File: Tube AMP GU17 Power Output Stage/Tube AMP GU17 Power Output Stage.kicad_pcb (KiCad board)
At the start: 2 copper layers, 100 x 50 mm, 37 parts, among them J1 AIN+, J10 BRN, J11 B+, J12 BLU, J13 F, J14 FH, J15 F, J16 B+, J17 +222V, J18 VC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

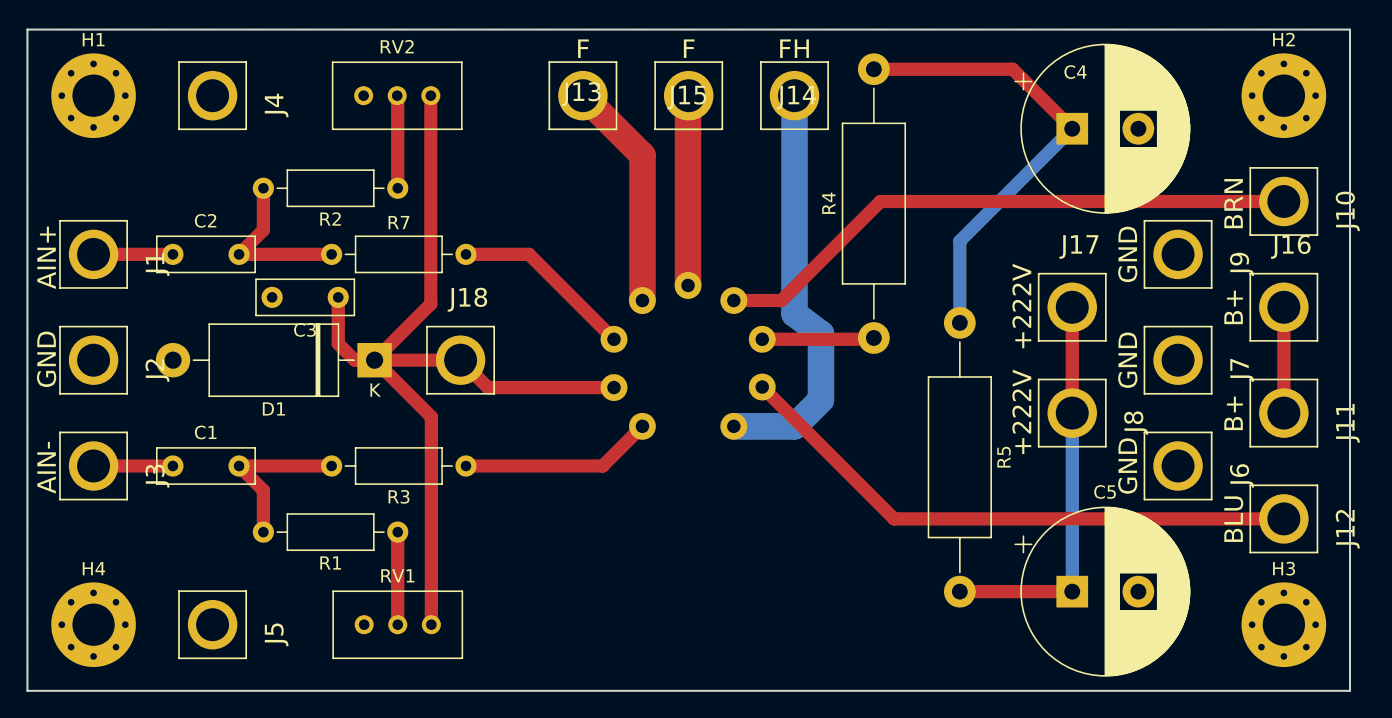
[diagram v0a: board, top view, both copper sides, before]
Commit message: Update to a new socket
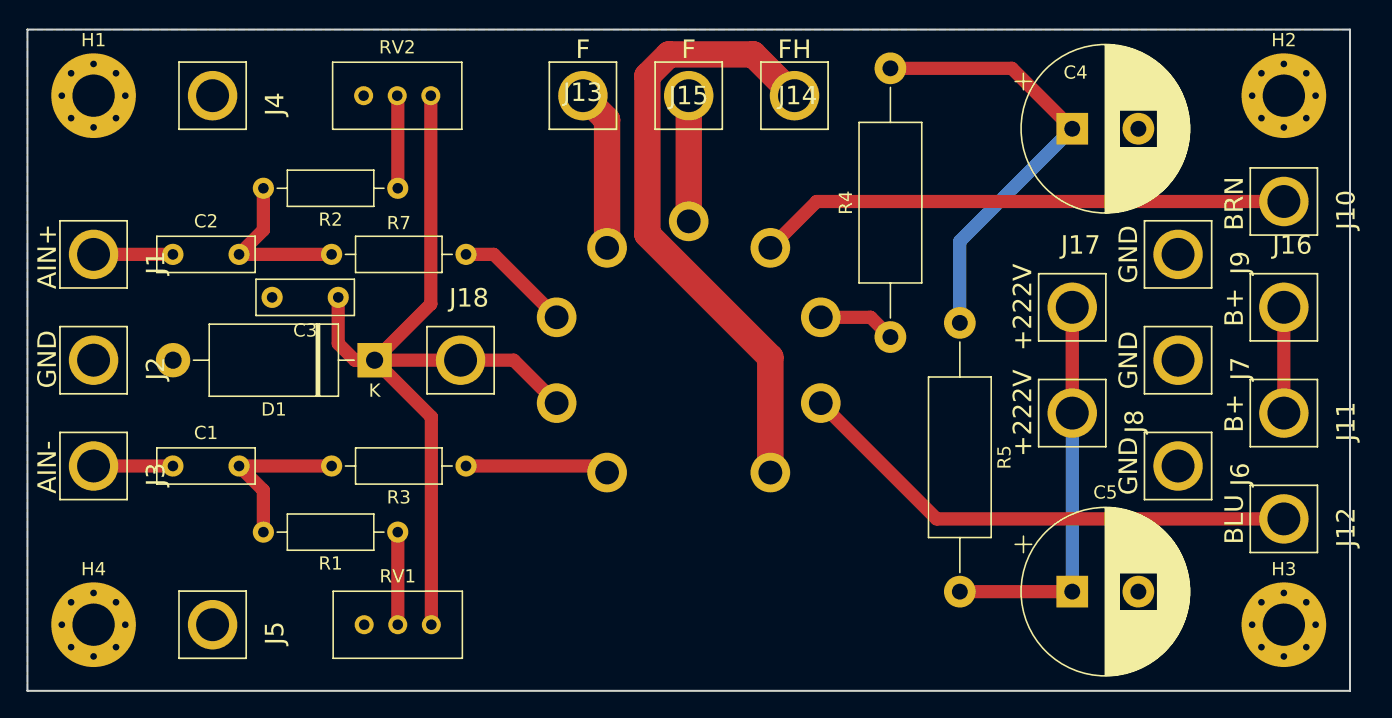
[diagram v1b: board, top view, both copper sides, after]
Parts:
- V1: footprint Valve:Valve_ECC-83-1 -> Tube Amp Parts:B9A-PCB-21
- moved V1 6.10 mm to (117.0, 97.0), turned to 0 degrees
- moved R4 1.25 mm to (132.2, 95.2)
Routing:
- net Net-(J14-Pad1): track 31.4 -> 46.9 mm
- net Net-(J13-Pad1): track 17.4 -> 12.3 mm
- net Net-(R7-Pad2): track 13.8 -> 8.82 mm
- net Net-(J12-Pad1): track 43.6 -> 38.6 mm
- net Net-(J15-Pad1): track 14.4 -> 9.50 mm
- net Net-(J10-Pad1): track 44.7 -> 40.3 mm
- net /+22V: track 69.3 -> 65.4 mm
- net Net-(R3-Pad1): track 14.6 -> 10.9 mm
- net Net-(R4-Pad1): track 8.48 -> 5.88 mm
- net Net-(C4-Pad1): track 35.1 -> 33.8 mm
